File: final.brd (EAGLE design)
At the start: 76 x 60.4 mm, 84 parts, among them IC2 MEGA8-AI, IC4 7805, Q2 32.768kHz, U2 DS1307

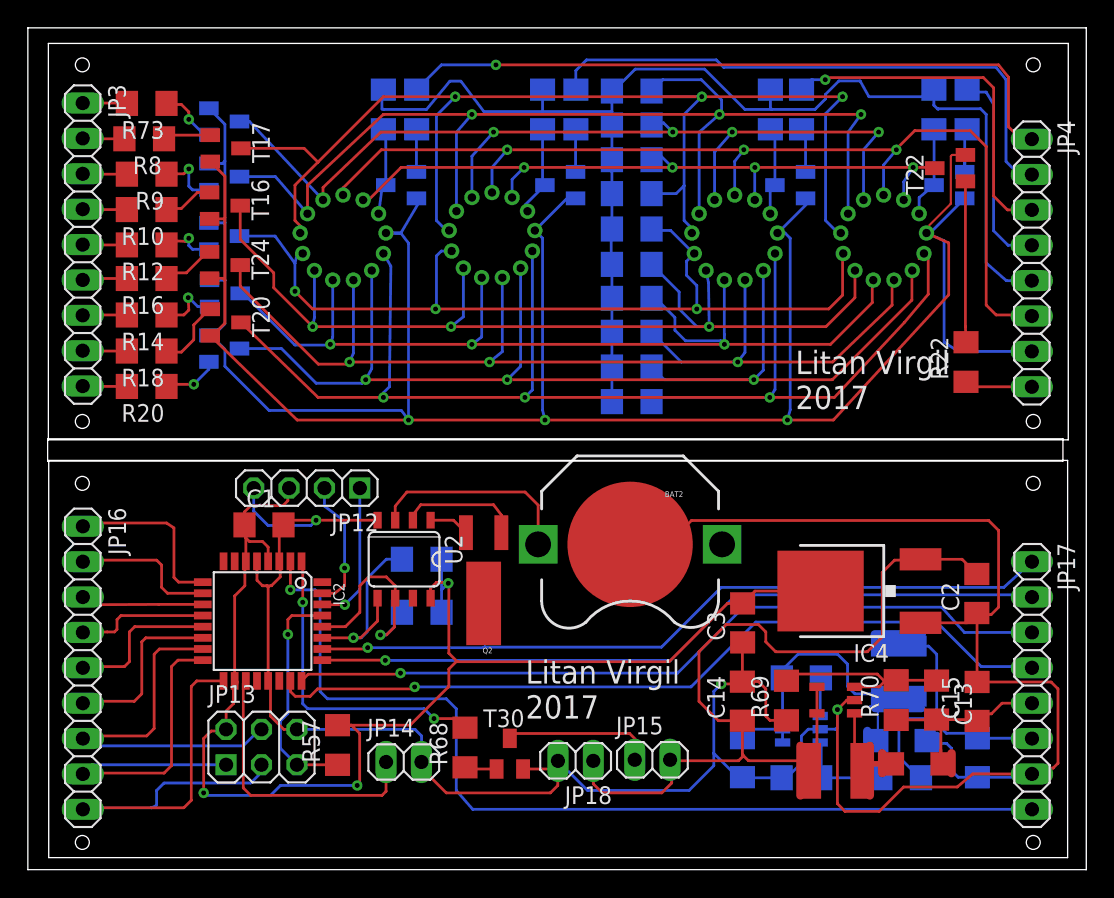
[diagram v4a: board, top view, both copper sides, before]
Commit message: moved 1k resisitors on logic board, more compact. fixed inductor, diode and 7805 packages. TODO add ground plane, move holes, add milling
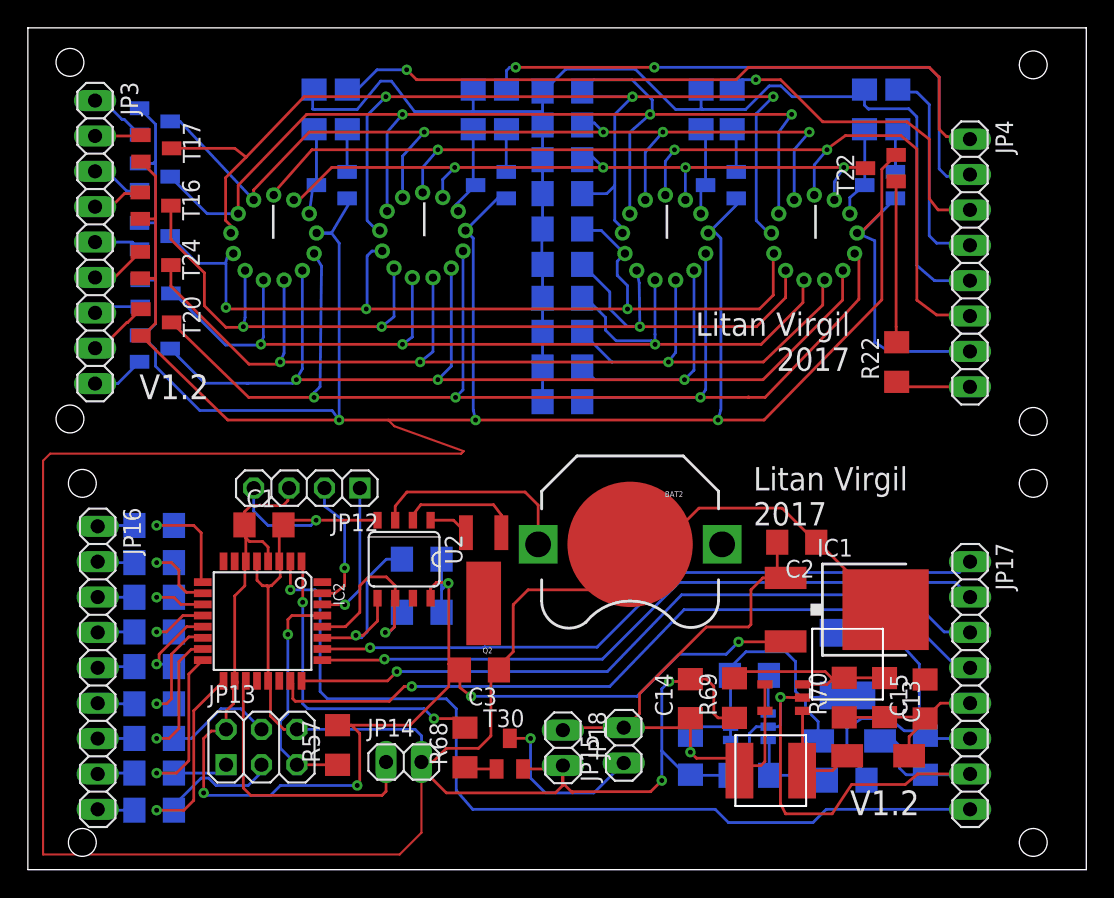
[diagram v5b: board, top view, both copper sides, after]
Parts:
- removed IC4: 7805, v-reg:DPACK
- removed R10, R12, R14, R16, R18, R20, R73, R8, R9: 1k, eagle-ltspice:R1206
- removed U$16, U$20: BYS10, BYS10-25:DO-214AC
- removed U$17: INDUCTOR, djnr5020:DJNR5020
- removed U$19: 15uH, djnr5020:DJNR5020
- added IC1: LD117ADT12TR, v-reg:DPACK
- added R24, R25, R26, R28, R30, R32, R33, R34, R35: 1k, eagle-ltspice:R1206
- added U$5, U$6: BYS10, BYS10-25:DO-214AC
- added U$7, U$8: 15uH, djnr5020:DJNR5020
- C13: value (none) -> 120pF
- C14, C15: value (none) -> 22uF
- C16: value 10uF -> 22uF
- C18: value 22uF -> 10uF
- R69: value (none) -> 13k
- R70: value (none) -> 200k
- R71, R72: value 1k -> 10k
- moved C3 19.2 mm to (32.4, 14.3), turned to 180 degrees
- moved C2 13.4 mm to (55.2, 23.5), turned to 180 degrees
- moved R31 4.98 mm to (60.1, 54.6)
- moved U$2 4.98 mm to (28.3, 45.5)
- moved R1 4.98 mm to (38.4, 53.5)
- moved R11 4.98 mm to (38.4, 51.0)
- moved R13 4.98 mm to (38.4, 36.1)
- moved R15 4.98 mm to (38.4, 38.6)
- moved R17 4.98 mm to (20.5, 54.6)
- moved R19 4.98 mm to (22.9, 54.6)
- moved R2 4.98 mm to (38.4, 43.5)
- moved R21 4.98 mm to (32.0, 54.6)
- moved R22 4.98 mm to (62.4, 36.4)
- moved R23 4.98 mm to (34.4, 54.6)
- moved R27 4.98 mm to (48.3, 54.6)
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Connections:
- removed net N$1: JP3.1, R73.2
- new net N$48: JP16.1, R24.1
- net +5V: now also IC1.3; no longer IC4.4
- net 1V5: now also U$8.P$1; no longer U$19.1
- net 20V: now also U$6.2; no longer U$16.2
- net GND: now also IC1.4, U$5.1; no longer IC4.1, U$20.1
- net MISO: now also R34.2; no longer JP16.8
- net MOSI: now also R32.2; no longer JP16.7
- net N$15: now also R33.2; no longer JP16.6
- net N$17: now also R30.2; no longer JP16.5
- net N$19: now also R28.2; no longer JP16.4
- net N$2: now also T17.B; no longer R8.2
- net N$21: now also R26.2; no longer JP16.3
- net N$26: now also JP3.1; no longer R73.1
- net N$27: now also JP16.3, R26.1; no longer R8.1, T17.B
- net N$28: now also JP3.3; no longer R9.1
- net N$29: now also JP3.4; no longer R10.1
- net N$3: now also JP16.9, R35.1; no longer JP3.3, R9.2
- net N$30: now also JP16.2, R25.1; no longer R12.1, T21.B
- net N$31: now also JP3.6; no longer R16.1
- net N$32: now also JP3.7; no longer R14.1
- net N$33: now also JP3.8; no longer R18.1
- net N$34: now also JP3.9; no longer R20.1
- net N$35: now also R25.2; no longer JP16.2
- net N$36: now also R24.2; no longer JP16.1
- net N$4: now also JP16.8, R34.1; no longer JP3.4, R10.2
- net N$5: now also T21.B; no longer R12.2
- net N$6: now also JP16.7, R32.1; no longer JP3.6, R16.2
- net N$7: now also JP16.6, R33.1; no longer JP3.7, R14.2
- net N$8: now also JP16.5, R30.1; no longer JP3.8, R18.2
- net N$9: now also JP16.4, R28.1; no longer JP3.9, R20.2
- net N$90: now also U$6.1, U$7.P$1; no longer U$16.1, U$17.1
- net N$93: now also U$5.2, U$8.P$2; no longer U$19.2, U$20.2
- net SCK: now also R35.2; no longer JP16.9
- net VCC: now also IC1.1, U$7.P$2; no longer IC4.3, U$17.2
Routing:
- net GND: track 393.2 -> 480.1 mm, vias 6 -> 7
- net VCC: track 69.6 -> 52.7 mm, vias 0 -> 1
- net SCK: track 34.0 -> 22.3 mm, vias 0 -> 1
- net MISO: track 26.7 -> 15.6 mm, vias 0 -> 1
- net MOSI: track 27.9 -> 17.8 mm, vias 0 -> 1
- net N$17: track 11.1 -> 6.06 mm, vias 0 -> 1
- net N$48: track 0.00 -> 4.64 mm
- net SELECT3: track 78.4 -> 73.9 mm
- net N$19: track 9.52 -> 5.04 mm, vias 0 -> 1
- net N$35: track 10.5 -> 6.09 mm, vias 0 -> 1
- net N$36: track 12.5 -> 8.25 mm, vias 0 -> 1
- net N$15: track 12.7 -> 8.45 mm, vias 0 -> 1
- net N$21: track 8.91 -> 4.77 mm, vias 0 -> 1
- net SELECT1: track 103.2 -> 99.5 mm
- net N$37: track 69.4 -> 65.7 mm
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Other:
- outline, holes or cut-outs redrawn
- board text added: "V1.2"
- board text added: "|"

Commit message: shrinkified driver board. not OK
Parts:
- removed R19, R22, R23, R29, R36: 1k, eagle-ltspice:R1206
- added R10, R12, R14, R8, R9: 1k, eagle-ltspice:R1206
- moved T22 15.0 mm to (58.1, 35.7), flipped to the bottom, turned to 0 degrees
- moved JP15 14.4 mm to (28.4, 9.10)
- moved T20 12.1 mm to (19.2, 32.4)
- moved R68 11.6 mm to (20.6, 4.71), flipped to the bottom, turned to 0 degrees
- moved T23 11.3 mm to (19.3, 32.4)
- moved T16 11.2 mm to (13.4, 37.4)
- moved T24 11.1 mm to (16.3, 34.9)
- moved BAT2 9.72 mm to (33.6, 24.3), turned to 0 degrees
- moved T19 9.69 mm to (16.3, 34.8)
- moved C13 9.60 mm to (51.9, 12.4)
- moved U$6 9.60 mm to (51.6, 8.18)
- moved U$7 9.60 mm to (43.7, 7.11)
- moved C14 9.60 mm to (38.0, 12.3)
- moved C15 9.60 mm to (54.8, 12.3)
- moved C16 9.60 mm to (38.0, 8.22)
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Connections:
- net 1.5V renamed 1.5VD
- removed net N$16: R19.1, T25.B
- removed net N$20: R23.1, T26.B
- removed net N$23: R29.1, T27.B
- removed net N$25: R36.1, T28.B
- removed net N$39: JP4.8, R22.1
- removed net SELECT4.1: JP4.4, R36.2
- new net 20VD: JP4.5, R1.2, R11.2, R13.2, R15.2, R17.2, R2.2, R21.2, R27.2, R3.2, R31.2, R4.2, R5.2, R6.2, R7.2
- new net N$11: JP17.1, R8.2
- new net N$12: JP17.2, R9.2
- new net N$13: JP17.3, R10.2
- new net N$40: JP17.4, R12.2
- new net N$41: JP17.8, R14.2
- new net SELECT1D: JP4.1, T25.B
- new net SELECT2D: JP4.2, T26.B
- new net SELECT3D: JP4.3, T27.B
- new net SELECT4.1D: JP4.4, T28.B
- net 20V: no longer JP4.5, R1.2, R11.2, R13.2, R15.2, R17.2, R2.2, R21.2, R27.2, R3.2, R31.2, R4.2, R5.2, R6.2, R7.2
- net N$37: now also R14.1; no longer JP17.8
- net N$38: now also JP4.8; no longer R22.2
- net SELECT1: now also R8.1; no longer JP17.1, JP4.1, R19.2
- net SELECT2: now also R10.1; no longer JP17.3, JP4.2, R23.2
- net SELECT3: now also R9.1; no longer JP17.2, JP4.3, R29.2
- net SELECT4: now also R12.1; no longer JP17.4
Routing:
- net 20V: track 107.9 -> 14.1 mm
- net 20VD: track 0.00 -> 90.6 mm, vias 0 -> 2
- net SELECT1: track 99.5 -> 34.7 mm, vias 2 -> 1
- net SELECT2: track 93.9 -> 35.1 mm, vias 3 -> 1
- net SELECT1D: track 0.00 -> 47.7 mm, vias 0 -> 1
- net SELECT2D: track 0.00 -> 44.1 mm, vias 0 -> 2
- net SELECT3: track 73.9 -> 33.9 mm, vias 2 -> 1
- net GND: track 480.1 -> 453.5 mm, vias 7 -> 11
- net SELECT3D: track 0.00 -> 21.6 mm, vias 0 -> 1
- net SELECT4: track 54.6 -> 37.0 mm
- net SELECT4.1D: track 0.00 -> 16.6 mm, vias 0 -> 1
- net N$37: track 65.7 -> 49.7 mm
- net SELECT4.1: track 15.3 -> 0.00 mm
- net SEGMENT-C: track 51.6 -> 65.9 mm
- net SEGMENT-DP: track 98.5 -> 87.9 mm
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
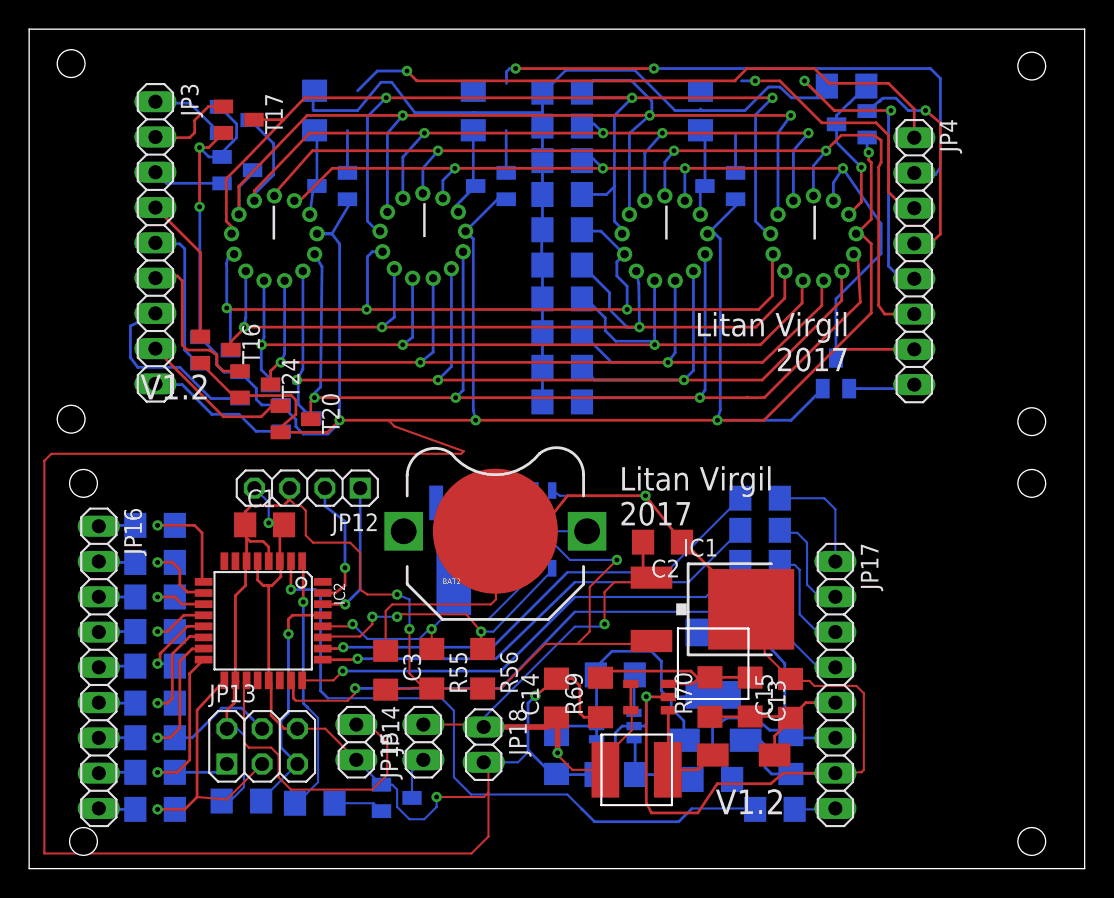
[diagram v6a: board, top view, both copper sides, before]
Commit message: driver board update, all components on bottom. still to large
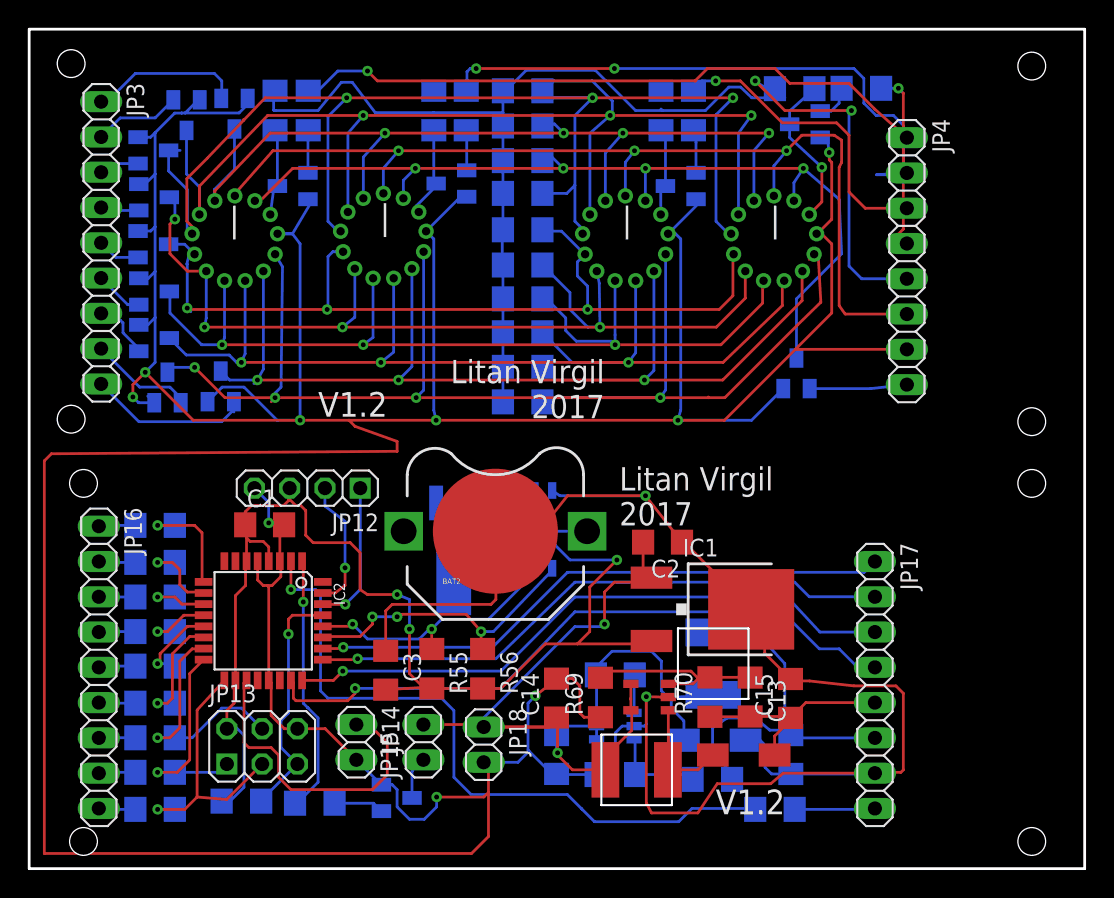
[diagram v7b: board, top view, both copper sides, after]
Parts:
- removed R12: 1k, eagle-ltspice:R1206
- added R16: 1k, eagle-ltspice:R1206
- moved R8 35.0 mm to (31.5, 54.6), turned to 90 degrees
- moved R10 34.9 mm to (59.9, 56.2)
- moved R9 30.6 mm to (47.8, 54.6), turned to 90 degrees
- moved T16 11.8 mm to (8.99, 48.3), flipped to the bottom, turned to 90 degrees
- moved T19 9.94 mm to (8.99, 41.6)
- moved T20 9.50 mm to (9.96, 34.6), flipped to the bottom, turned to 0 degrees
- moved T21 8.84 mm to (8.94, 45.0)
- moved T24 8.01 mm to (8.99, 38.2), flipped to the bottom, turned to 90 degrees
- moved R3 7.99 mm to (35.5, 56.0)
- moved R4 7.83 mm to (35.5, 48.6)
- moved T18 6.21 mm to (8.94, 51.7)
- moved T23 5.92 mm to (13.8, 34.7), turned to 0 degrees
- moved JP3 3.91 mm to (5.18, 45.1)
- moved T17 3.77 mm to (11.3, 54.3), flipped to the bottom, turned to 180 degrees
- moved R31 3.74 mm to (55.1, 56.2)
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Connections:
- removed net N$31: JP3.6, T24.B
- removed net N$32: JP3.7, T19.B
- removed net N$40: JP17.4, R12.2
- new net N$16: JP4.4, R10.2
- new net N$20: JP3.7, T24.B
- new net N$23: JP3.6, T19.B
- net N$11: now also JP4.1, R16.2; no longer JP17.1, R8.2
- net N$12: now also JP4.2, R8.2; no longer JP17.2, R9.2
- net N$13: now also JP4.3, R9.2; no longer JP17.3, R10.2
- net SEGMENT-D: now also R3.1, T17.C; no longer R4.1, T18.C
- net SEGMENT-E: now also R4.1, T18.C; no longer R3.1, T17.C
- net SELECT1: now also JP17.1; no longer R8.1
- net SELECT1D: now also R16.1; no longer JP4.1
- net SELECT2: now also JP17.3; no longer R10.1
- net SELECT2D: now also R8.1; no longer JP4.2
- net SELECT3: now also JP17.2; no longer R9.1
- net SELECT3D: now also R9.1; no longer JP4.3
- net SELECT4: now also JP17.4; no longer R12.1
- net SELECT4.1D: now also R10.1; no longer JP4.4
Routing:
- net SELECT1D: track 47.7 -> 3.67 mm, vias 1 -> 0
- net SELECT2D: track 44.1 -> 2.87 mm, vias 2 -> 0
- net N$11: track 8.09 -> 46.4 mm, vias 0 -> 1
- net N$12: track 7.75 -> 43.1 mm, vias 0 -> 2
- net SELECT3D: track 21.6 -> 3.14 mm, vias 1 -> 0
- net N$16: track 0.00 -> 14.3 mm, vias 0 -> 1
- net N$13: track 7.95 -> 22.1 mm, vias 0 -> 1
- net SELECT4.1D: track 16.6 -> 2.74 mm, vias 1 -> 0
- net N$32: track 13.5 -> 0.00 mm
- net GND: track 453.5 -> 466.5 mm
- net N$31: track 12.1 -> 0.00 mm
- net SELECT2: track 35.1 -> 46.1 mm
- net SELECT4: track 37.0 -> 47.9 mm
- net SELECT3: track 33.9 -> 43.6 mm
- net N$5: track 11.1 -> 3.09 mm
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
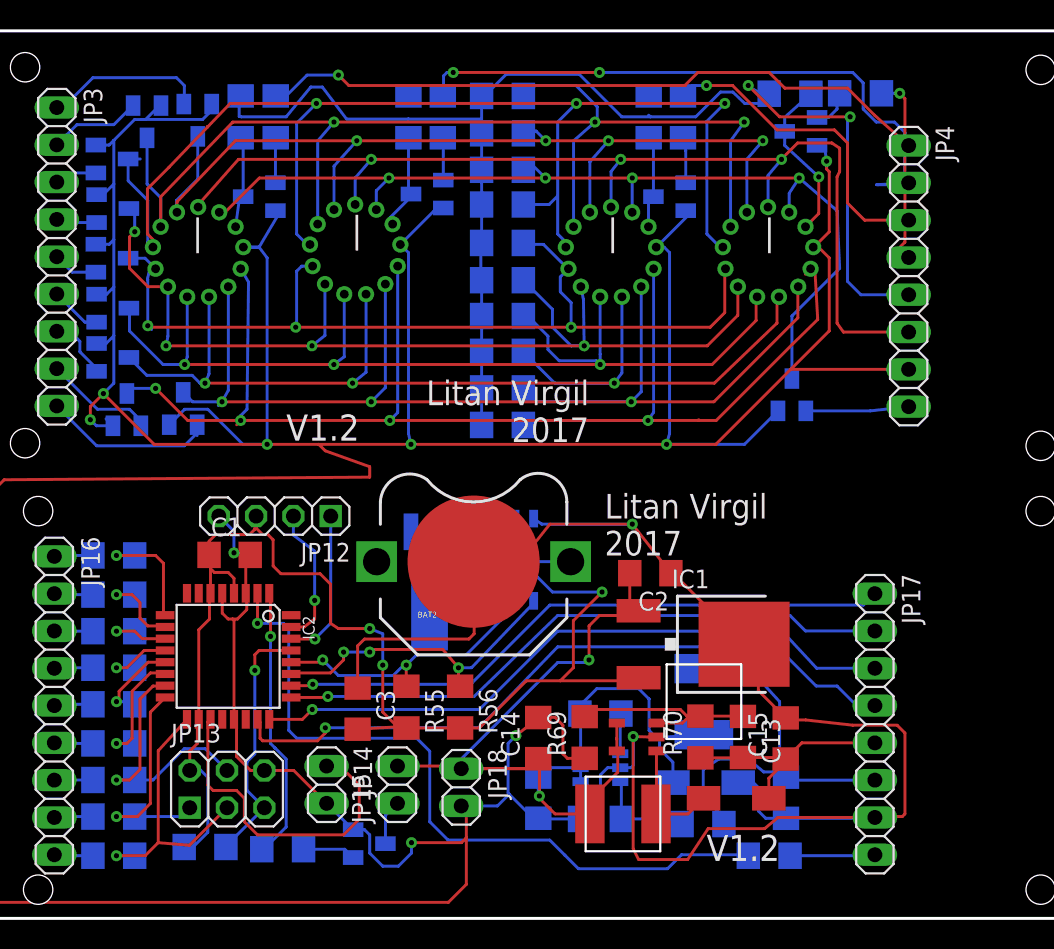
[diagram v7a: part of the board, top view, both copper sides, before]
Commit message: thicker power-lines, smaller driver
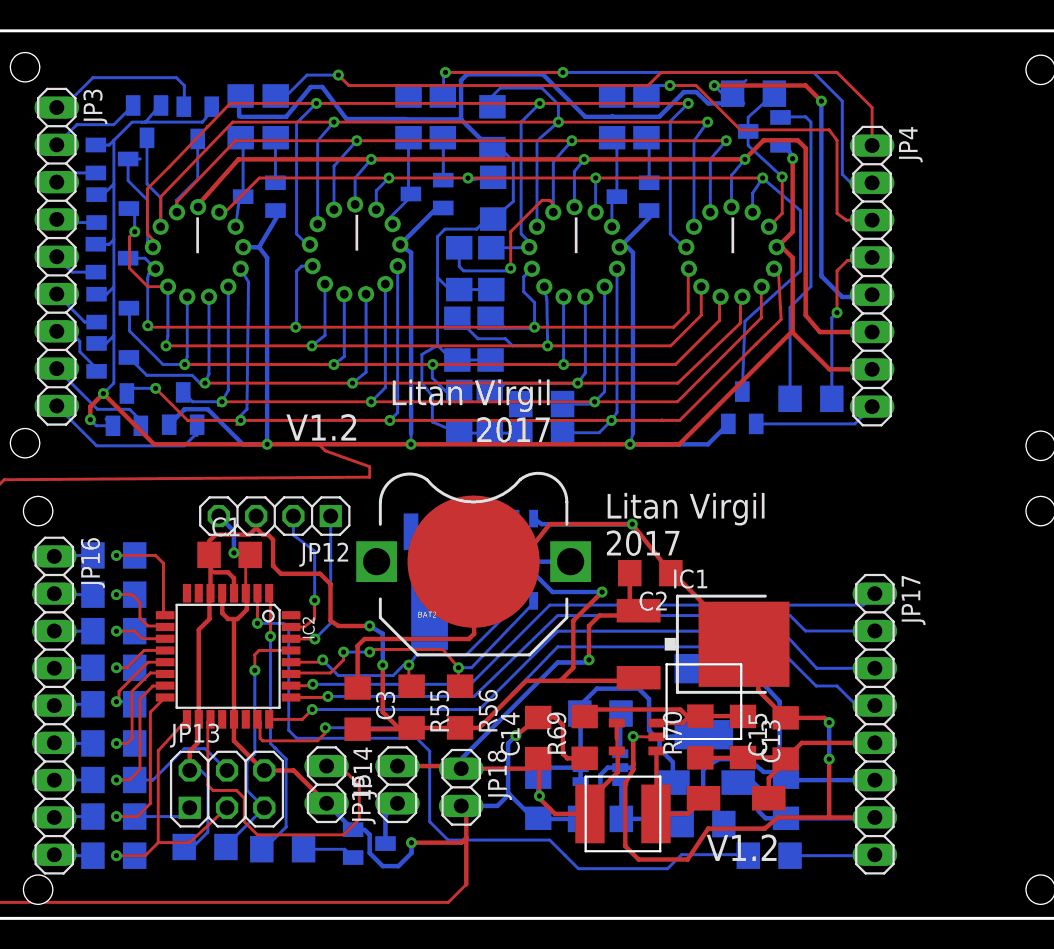
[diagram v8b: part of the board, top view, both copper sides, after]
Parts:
- moved R10 21.1 mm to (56.5, 35.4)
- moved R1 9.68 mm to (32.6, 44.2), turned to 270 degrees
- moved R5 7.19 mm to (32.6, 34.5), turned to 270 degrees
- moved R7 6.60 mm to (34.7, 39.4), turned to 270 degrees
- moved R2 5.05 mm to (32.5, 39.4), turned to 270 degrees
- moved R4 4.43 mm to (34.8, 44.2), turned to 270 degrees
- moved R15 4.20 mm to (34.7, 34.5), turned to 270 degrees
- moved T22 3.49 mm to (51.9, 34.8)
- moved R13 2.87 mm to (38.2, 35.0)
- moved R6 2.72 mm to (38.2, 33.1)
- moved R31 2.49 mm to (52.6, 56.2)
- moved R9 2.49 mm to (45.3, 54.6)
- moved T27 2.49 mm to (44.4, 49.1)
- moved U$3 2.49 mm to (40.4, 45.3)
- moved JP4 2.49 mm to (60.7, 43.7)
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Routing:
- net 20VD: track 94.2 -> 113.9 mm
- net SELECT4.1D: track 2.74 -> 21.7 mm
- net GND: track 466.5 -> 455.2 mm, vias 11 -> 13
- net SEGMENT-B: track 79.3 -> 71.4 mm
- net SEGMENT-G: track 65.9 -> 73.3 mm
- net SEGMENT-DP: track 95.4 -> 88.0 mm
- net SEGMENT-H: track 70.6 -> 63.2 mm, vias 3 -> 4
- net N$12: track 43.1 -> 37.1 mm
- net SEGMENT-A: track 74.2 -> 71.0 mm
- net 1.5VD: track 73.3 -> 70.5 mm
- net SEGMENT-Q: track 63.0 -> 60.1 mm
- net N$16: track 14.3 -> 11.6 mm
- net SEGMENT-F: track 68.7 -> 66.4 mm
- net SEGMENT-E: track 91.9 -> 89.7 mm
- net SEGMENT-C: track 66.2 -> 64.6 mm
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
